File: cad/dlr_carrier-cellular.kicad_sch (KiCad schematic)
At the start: 13 parts, among them J6 U.FL, J7 SIM, U3 BG770A-NA, U4 TXS0108E

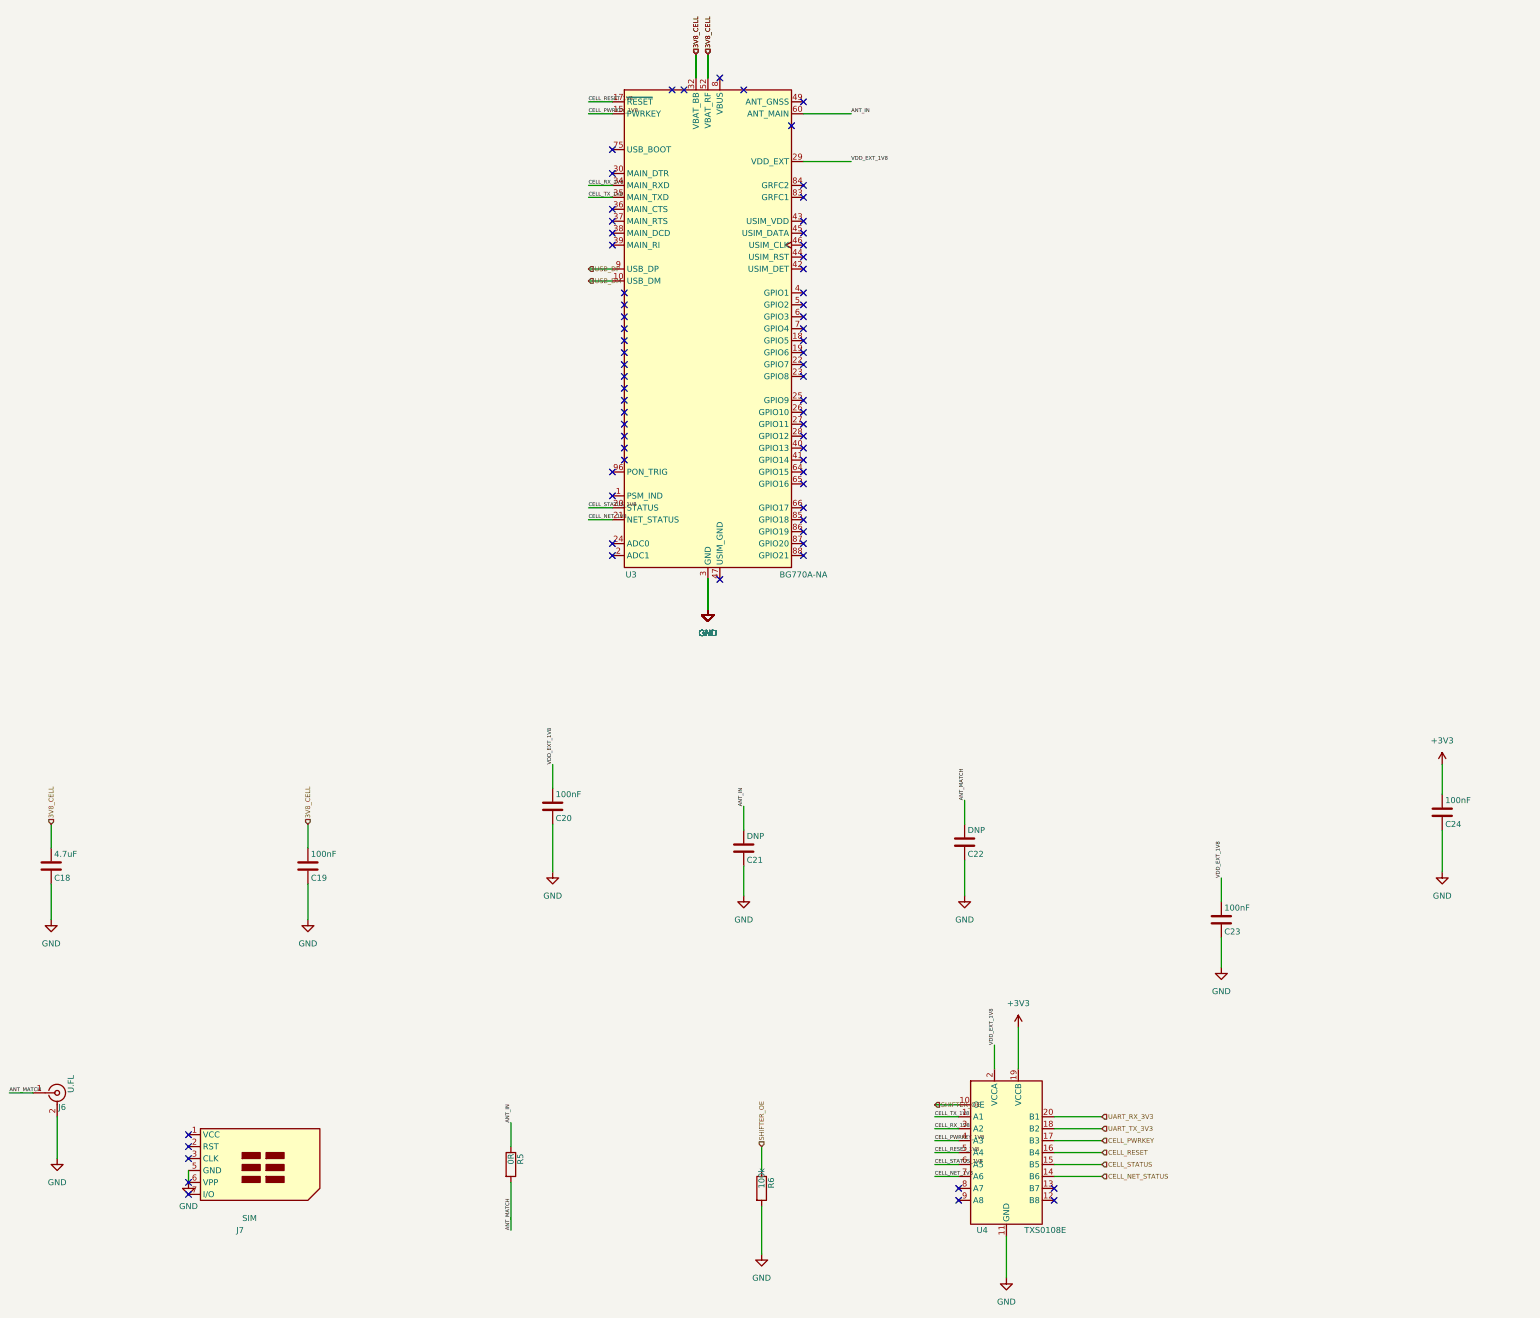
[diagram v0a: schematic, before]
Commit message: 🎨 style: lint fixes (f-string, unused imports, complexity, naming)
CI lint surface from the prior commit:
* F541: drop extraneous `f` prefixes on f-strings without placeholders
* F401: remove unused `math` and `_place_pwr_flags` imports
* C901: extract `_route_sheet_nets` helper so `build_child_sheet`
  complexity drops back under the McCabe threshold
* N806: lowercase local constants in `build_root_sheet`
* black: reformat multi_sheet.py + schematic.py

Co-Authored-By: Claude Opus 4.7 (1M context) <noreply@anthropic.com>
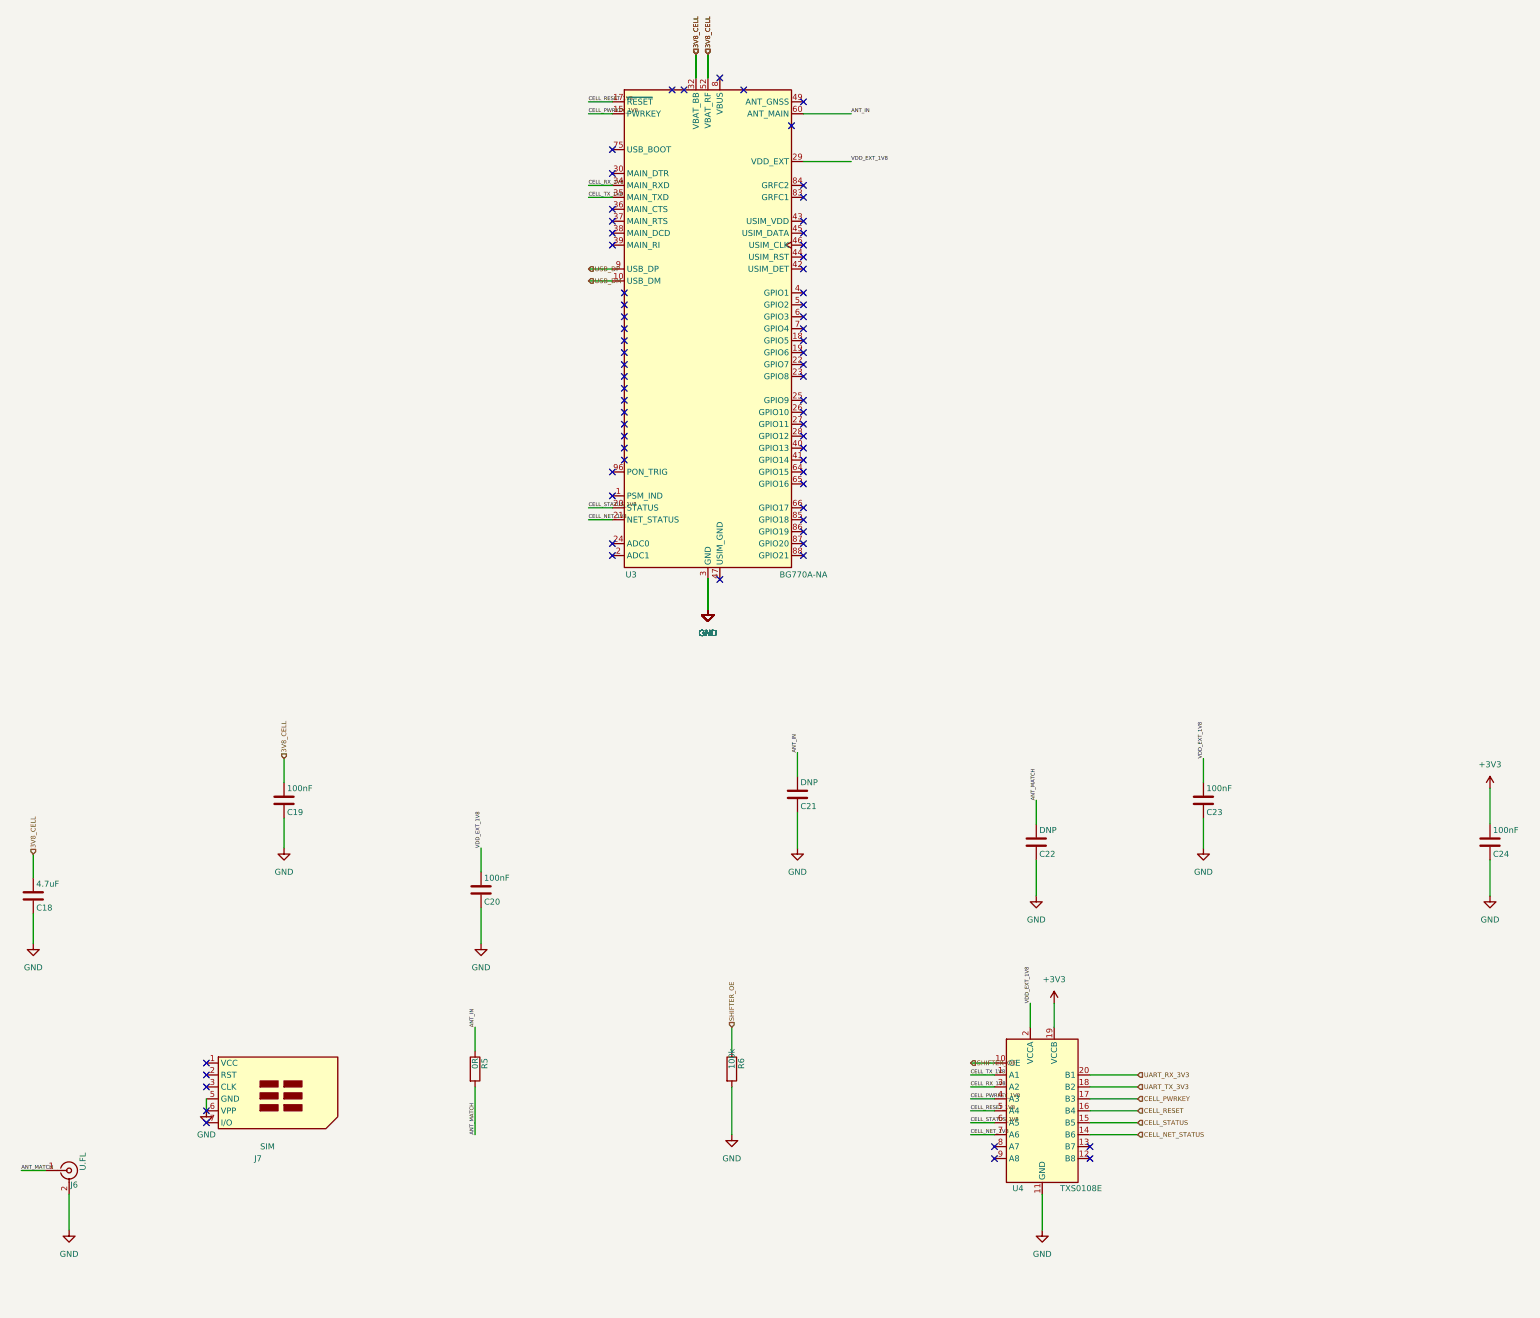
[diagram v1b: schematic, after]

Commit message: 🪪 feat(anemometer): low-wind variant — Vaisala WMT702, kit SKU split
Locks the low-wind variant per the grill-me design tree. Single PCB +
single firmware binary; the variant lives in the kit BOM (sensor + cable
harness + PV panel + battery). Both sensors speak NMEA 0183 over the
RS-485 transceiver so the driver is talker-agnostic.

Hardware:
* anemometer.py: add SMBJ24CA TVS on V+→GND for IEC 61000-4-5 2 kV
  surge tolerance (utility-tower deployment).

Theory:
* theory.ipynb §6: variant-aware power-budget cell. WMT702's 480 mW
  draw needs a 30 W panel + 100 Wh battery to hold 1.66× winter margin
  and 2.22 d autonomy. High-wind kit (Calypso, 1 mW) stays on the
  existing 20 W / 50 Wh baseline.
* Expected-values table rebuilt with per-variant rows.

README:
* New "Anemometer Variants" section: full kit BOM table, deployment
  decision rule (NREL WIND Toolkit climatology, 15 % yr V_w<1 m/s
  threshold), fallback policy, per-variant power numbers.

Co-Authored-By: Claude Opus 4.7 (1M context) <noreply@anthropic.com>
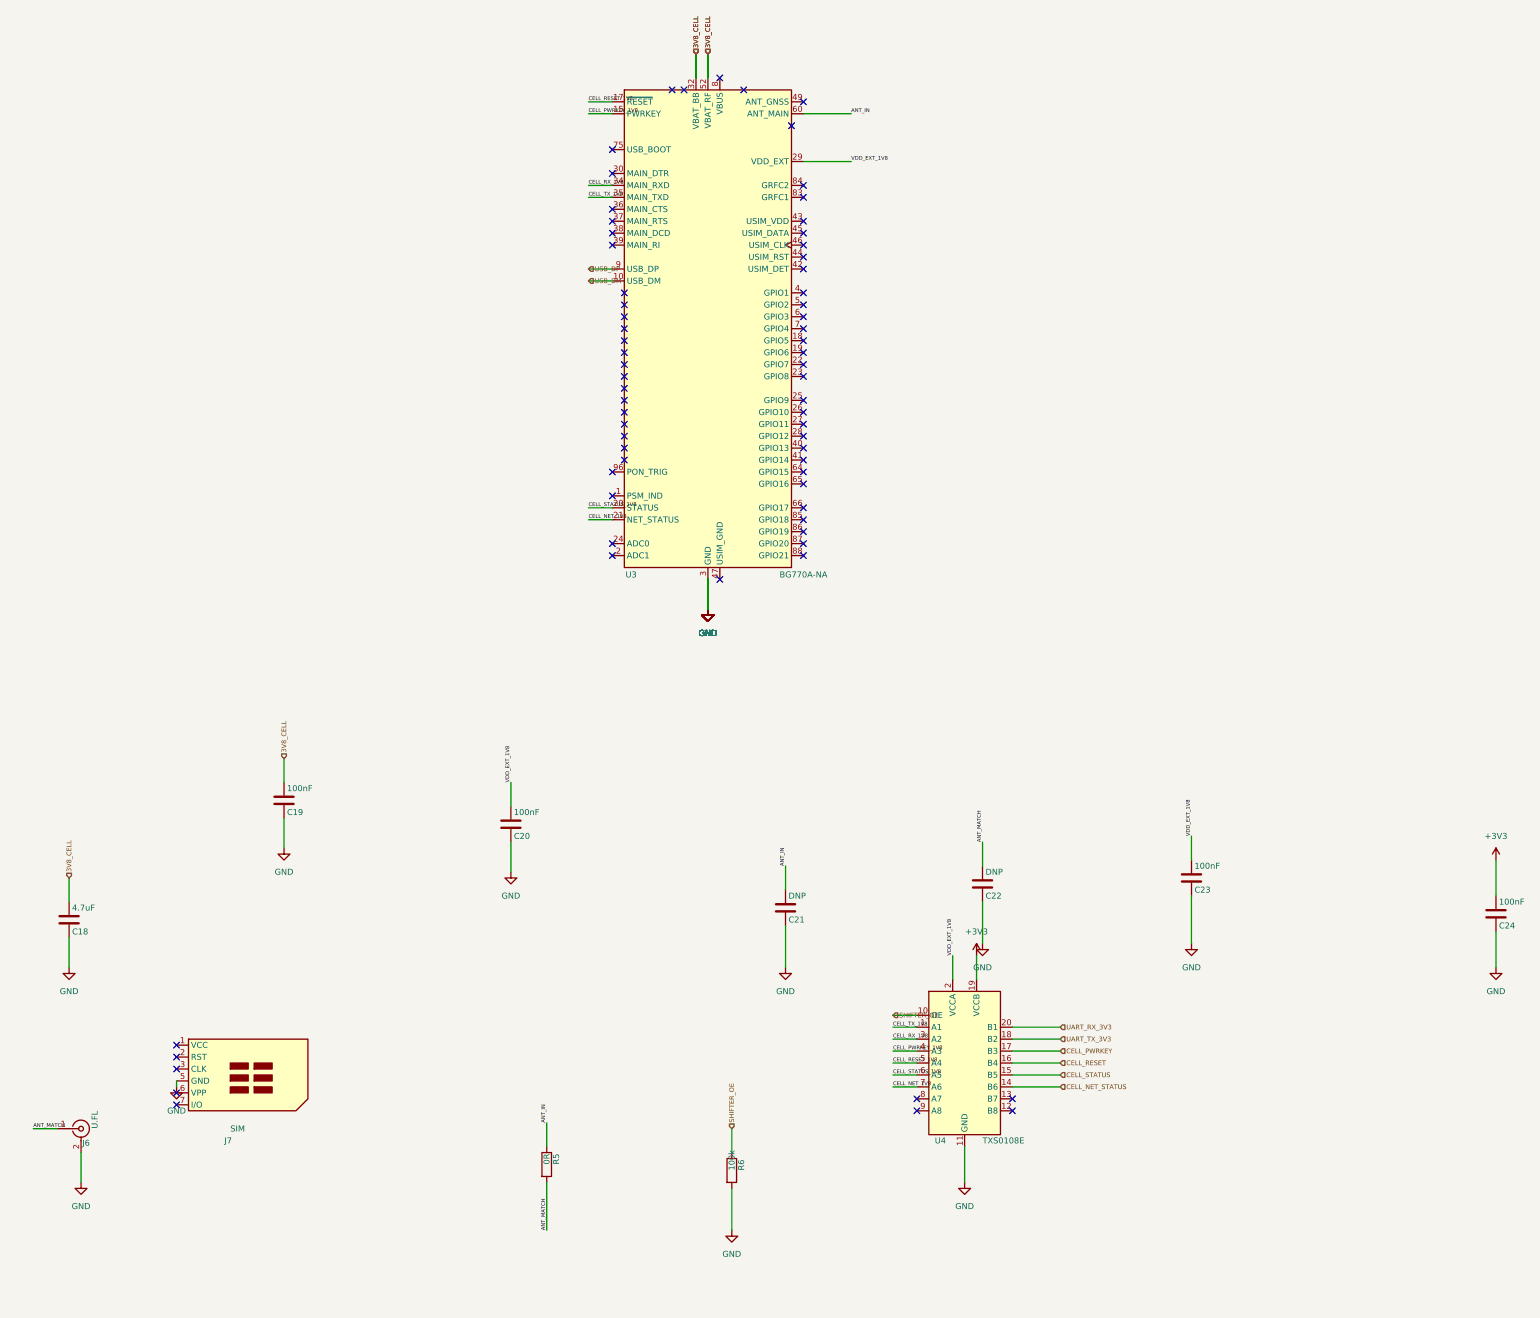
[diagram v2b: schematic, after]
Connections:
- net GND: no longer J7.6 (VPP)
